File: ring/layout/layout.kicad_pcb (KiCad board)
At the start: 2 copper layers, 31 parts, among them U1 ?, U10 ?, U11 ?, U2 ?, U3 ?, U4 ?, U5 ?, U6 ?, U7 ?, U8 ?, U9 ?, Y1 38.4MHz

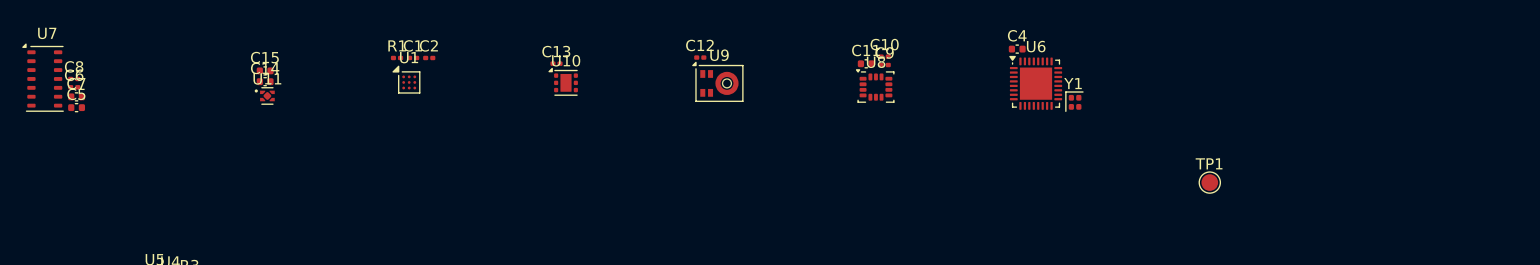
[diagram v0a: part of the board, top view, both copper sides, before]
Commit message: added in rf power
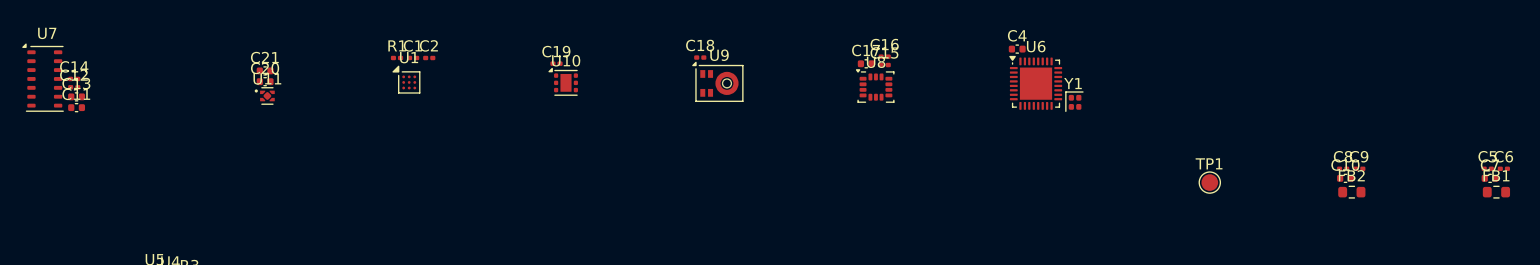
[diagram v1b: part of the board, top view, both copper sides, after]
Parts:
- added C10: 1uF, C_0402_1005Metric:C_0402_1005Metric, F.Cu at (292.2, 114.5)
- added C5: 120pF, C_0201_0603Metric:C_0201_0603Metric, F.Cu at (305.0, 113.6)
- added C6: 100nF, C_0201_0603Metric:C_0201_0603Metric, F.Cu at (306.5, 113.6)
- added C7: 1uF, C_0402_1005Metric:C_0402_1005Metric, F.Cu at (305.3, 114.5)
- added C8: 120pF, C_0201_0603Metric:C_0201_0603Metric, F.Cu at (292.0, 113.6)
- added C9: 100nF, C_0201_0603Metric:C_0201_0603Metric, F.Cu at (293.5, 113.6)
- added FB1: 0 0Hz, R_0603_1608Metric:R_0603_1608Metric, F.Cu at (305.8, 115.7)
- added FB2: 0 0Hz, R_0603_1608Metric:R_0603_1608Metric, F.Cu at (292.8, 115.7)
- renumbered C5 to C11, C6 to C12, C7 to C13, C8 to C14, C9 to C15, C10 to C16, C11 to C17, C12 to C18, C13 to C19, C14 to C20, C15 to C21
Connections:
- net cpu.N259 renamed cpu.N337
- net cpu.N260 renamed cpu.N338
- net cpu.N264 renamed cpu.N342
- U6 pad 10: GND -> cpu.N360
- U6 pad 13: GND -> cpu.N361
- U6 pad 25: GND -> cpu.N392

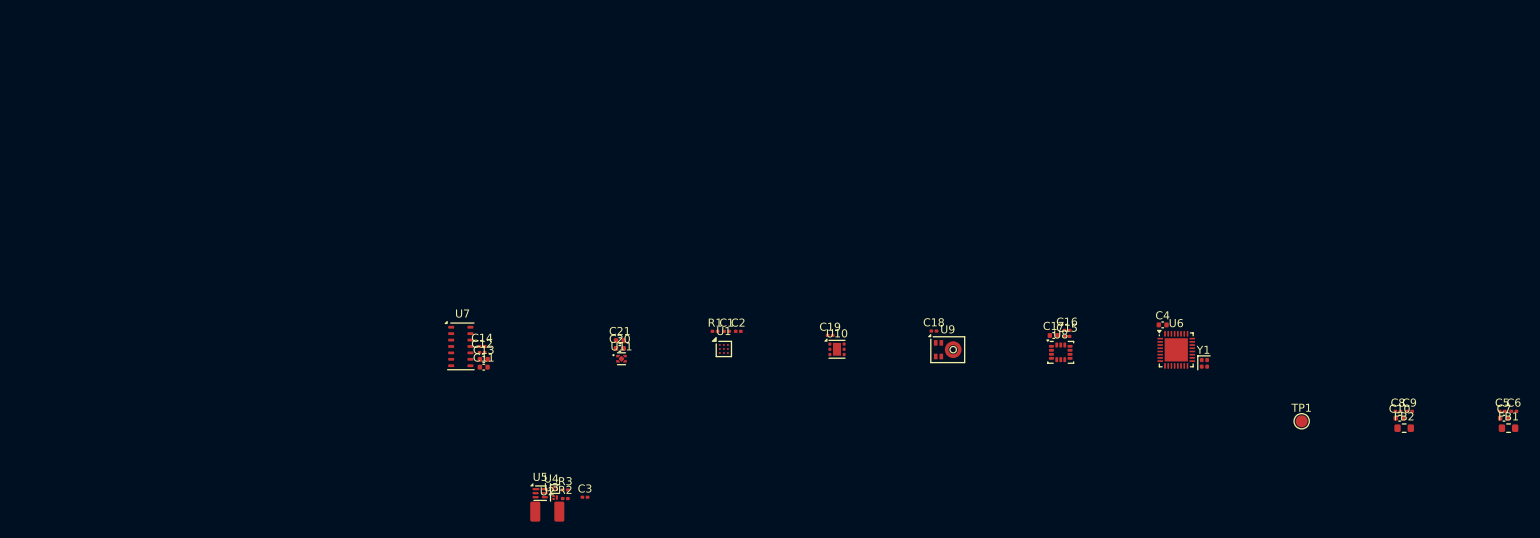
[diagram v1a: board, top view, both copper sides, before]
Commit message: finished port and antenna in zener
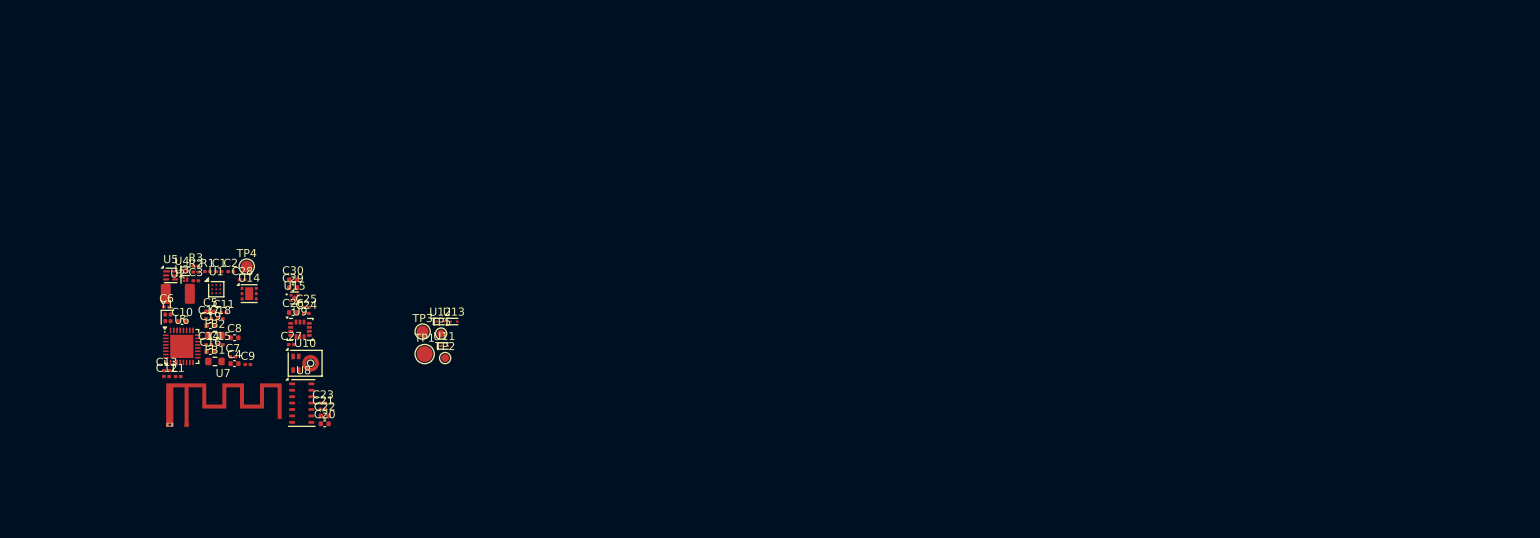
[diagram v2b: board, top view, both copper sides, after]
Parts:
- added C22: 4.7uF, C_0402_1005Metric:C_0402_1005Metric, F.Cu at (158.3, 114.2)
- added C23: 100nF, C_0201_0603Metric:C_0201_0603Metric, F.Cu at (158.0, 112.6)
- added C24: 100nF, C_0201_0603Metric:C_0201_0603Metric, F.Cu at (156.0, 101.4)
- added C25: 100nF, C_0201_0603Metric:C_0201_0603Metric, F.Cu at (156.0, 100.7)
- added C26: 1uF, C_0402_1005Metric:C_0402_1005Metric, F.Cu at (154.3, 101.3)
- added C27: 100nF, C_0201_0603Metric:C_0201_0603Metric, F.Cu at (154.1, 105.3)
- added C28: 100nF, C_0201_0603Metric:C_0201_0603Metric, F.Cu at (148.0, 97.2)
- added C29: 1uF, C_0402_1005Metric:C_0402_1005Metric, F.Cu at (154.3, 98.2)
- added C30: 1uF, C_0402_1005Metric:C_0402_1005Metric, F.Cu at (154.3, 97.3)
- added L1: 3.2nH, L_0201_0603Metric:L_0201_0603Metric, F.Cu at (140.0, 109.3)
- added TP2: , TestPoint_Pad_D1.0mm:TestPoint_Pad_D1.0mm, F.Cu at (173.3, 107.0)
- added TP3: , TestPoint_Pad_D1.5mm:TestPoint_Pad_D1.5mm, F.Cu at (170.5, 103.7)
- added TP4: , TestPoint_Pad_D1.0mm:TestPoint_Pad_D1.0mm, F.Cu at (148.5, 95.6)
- added TP5: , TestPoint_Pad_D1.0mm:TestPoint_Pad_D1.0mm, F.Cu at (172.8, 104.0)
- added U12: ?, D_SOD-923:D_SOD-923, F.Cu at (172.7, 102.5)
- added U13: ?, D_SOD-923:D_SOD-923, F.Cu at (174.4, 102.5)
- added U14: ?, WSON-6-1EP_2x2mm_P0.65mm_EP1x1.6mm:WSON-6-1EP_2x2mm_P0.65mm_EP1x1.6mm, F.Cu at (148.8, 99.0)
- added U15: ?, Texas_X2SON-4_1x1mm_P0.65mm:Texas_X2SON-4_1x1mm_P0.65mm, F.Cu at (154.5, 99.5)
- C11: value 10uF -> 100nF; footprint C_0402_1005Metric:C_0402_1005Metric -> C_0201_0603Metric:C_0201_0603Metric
- C12: value 100nF -> 1.6pF
- C13: value 4.7uF -> 18pF; footprint C_0402_1005Metric:C_0402_1005Metric -> C_0201_0603Metric:C_0201_0603Metric
- C14: value 100nF -> 120pF
- C16, C19: value 100nF -> 1uF; footprint C_0201_0603Metric:C_0201_0603Metric -> C_0402_1005Metric:C_0402_1005Metric
- C17: value 1uF -> 120pF; footprint C_0402_1005Metric:C_0402_1005Metric -> C_0201_0603Metric:C_0201_0603Metric
- C20: value 1uF -> 10uF
- C21, C7: value 1uF -> 100nF; footprint C_0402_1005Metric:C_0402_1005Metric -> C_0201_0603Metric:C_0201_0603Metric
- C5: value 120pF -> 10uF; footprint C_0201_0603Metric:C_0201_0603Metric -> C_0402_1005Metric:C_0402_1005Metric
- C8: value 120pF -> 1uF; footprint C_0201_0603Metric:C_0201_0603Metric -> C_0402_1005Metric:C_0402_1005Metric
- C9: value 100nF -> 10nF
- TP1: footprint TestPoint_Pad_D1.5mm:TestPoint_Pad_D1.5mm -> TestPoint_Pad_D2.0mm:TestPoint_Pad_D2.0mm
- U10: footprint WSON-6-1EP_2x2mm_P0.65mm_EP1x1.6mm:WSON-6-1EP_2x2mm_P0.65mm_EP1x1.6mm -> Infineon_PG-LLGA-5-1:Infineon_PG-LLGA-5-1
- U11: footprint Texas_X2SON-4_1x1mm_P0.65mm:Texas_X2SON-4_1x1mm_P0.65mm -> D_SOD-923:D_SOD-923
- U7: footprint Maxim_OLGA-14_3.3x5.6mm_P0.8mm:Maxim_OLGA-14_3.3x5.6mm_P0.8mm -> Texas_SWRA117D_2.4GHz_Right:Texas_SWRA117D_2.4GHz_Right
- U8: footprint LGA-14_3x2.5mm_P0.5mm_LayoutBorder3x4y:LGA-14_3x2.5mm_P0.5mm_LayoutBorder3x4y -> Maxim_OLGA-14_3.3x5.6mm_P0.8mm:Maxim_OLGA-14_3.3x5.6mm_P0.8mm
- U9: footprint Infineon_PG-LLGA-5-1:Infineon_PG-LLGA-5-1 -> LGA-14_3x2.5mm_P0.5mm_LayoutBorder3x4y:LGA-14_3x2.5mm_P0.5mm_LayoutBorder3x4y
- moved C6 168.5 mm to (138.5, 100.6)
- moved C5 161.5 mm to (144.0, 101.2)
- moved FB1 161.5 mm to (144.6, 107.4)
- moved C7 158.6 mm to (146.8, 106.8)
- moved C10 152.2 mm to (140.5, 102.4)
- moved FB2 148.7 mm to (144.6, 104.2)
- moved C8 145.3 mm to (147.0, 104.5)
- moved C9 144.9 mm to (148.7, 107.8)
- moved Y1 129.3 mm to (138.7, 102.0)
- moved U6 124.0 mm to (140.4, 105.6)
- moved C4 115.8 mm to (147.0, 107.7)
- moved TP1 109.6 mm to (170.7, 106.5)
- moved C16 106.8 mm to (144.0, 106.2)
- moved C15 105.6 mm to (145.2, 105.3)
- moved C17 105.4 mm to (143.8, 102.1)
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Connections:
- net N56 renamed N64
- net batman.N85 renamed batman.N93
- net batman.N86 renamed batman.N94
- net battery.N43 renamed battery.N51
- net battery.N44 renamed battery.N52
- net battery.N45 renamed battery.N53
- net battery.N46 renamed battery.N54
- net battery.N47 renamed battery.N55
- net battery.N48 renamed battery.N56
- net battery.N49 renamed battery.N57
- net cpu.N337 renamed cpu.N394
- net cpu.N338 renamed cpu.N395
- net cpu.N342 renamed cpu.N399
- net cpu.N392 renamed cpu.N498
- C10 pad 1: cpu.N360 -> VDD
- C11 pad 1: VBATT -> VDD
- C12 pad 1: VBATT -> cpu.ant.N487
- C13 pad 1: VDD -> cpu.ant.N488
- C13 pad 2: GND -> cpu.ant.N489
- C14 pad 1: VDD -> cpu.N418
- C15 pad 1: VDD -> cpu.N418
- C16 pad 1: VDD -> cpu.N418
- C17 pad 1: VDD -> cpu.N417
- C18 pad 1: VDD -> cpu.N417
- C19 pad 1: VDD -> cpu.N417
- C21 pad 1: VDD -> VBATT
- C5 pad 1: cpu.N361 -> VDD
- C6 pad 1: cpu.N361 -> VDD
- C7 pad 1: cpu.N361 -> VDD
- C8 pad 1: cpu.N360 -> VDD
- C9 pad 1: cpu.N360 -> VDD
- FB1 pad 2: cpu.N361 -> cpu.N418
- FB2 pad 2: cpu.N360 -> cpu.N417
- U10 pad 1: SCL -> N174
- U10 pad 2: GND -> VDD
- U10 pad 3: N111 -> N173
- U10 pad 5: VDD -> GND
- U11 pad 1: VDD -> VBATT
- U6 pad 10: cpu.N360 -> cpu.N417
- U6 pad 12: GND -> cpu.N463
- U6 pad 13: cpu.N361 -> cpu.N418
- U6 pad 31: N165 -> N173
- U6 pad 32: N166 -> N174
- U7 pad 1: hbt.N137 -> cpu.ant.N489
- U7 pad 2: SCL -> GND
- U8 pad 1: GND -> hbt.N145
- U8 pad 10: imu.N217 -> VBATT
- U8 pad 11: imu.N218 -> VDD
- U8 pad 12: VDD -> GND
- U8 pad 13: SCL -> N119
- U8 pad 14: SDA -> hbt.N145
- U8 pad 2: GND -> SCL
- U8 pad 3: GND -> SDA
- U8 pad 4: N187 -> GND
- U8 pad 5: VDD -> hbt.N145
- U8 pad 6: GND -> hbt.N145
- U8 pad 7: GND -> hbt.N145
- U8 pad 8: VDD -> hbt.N145
- U8 pad 9: N188 -> VBATT
- U9 pad 1: N166 -> GND
- U9 pad 2: VDD -> GND
- U9 pad 3: N165 -> GND
- U9 pad 4: GND -> N195
- U9 pad 5: GND -> VDD

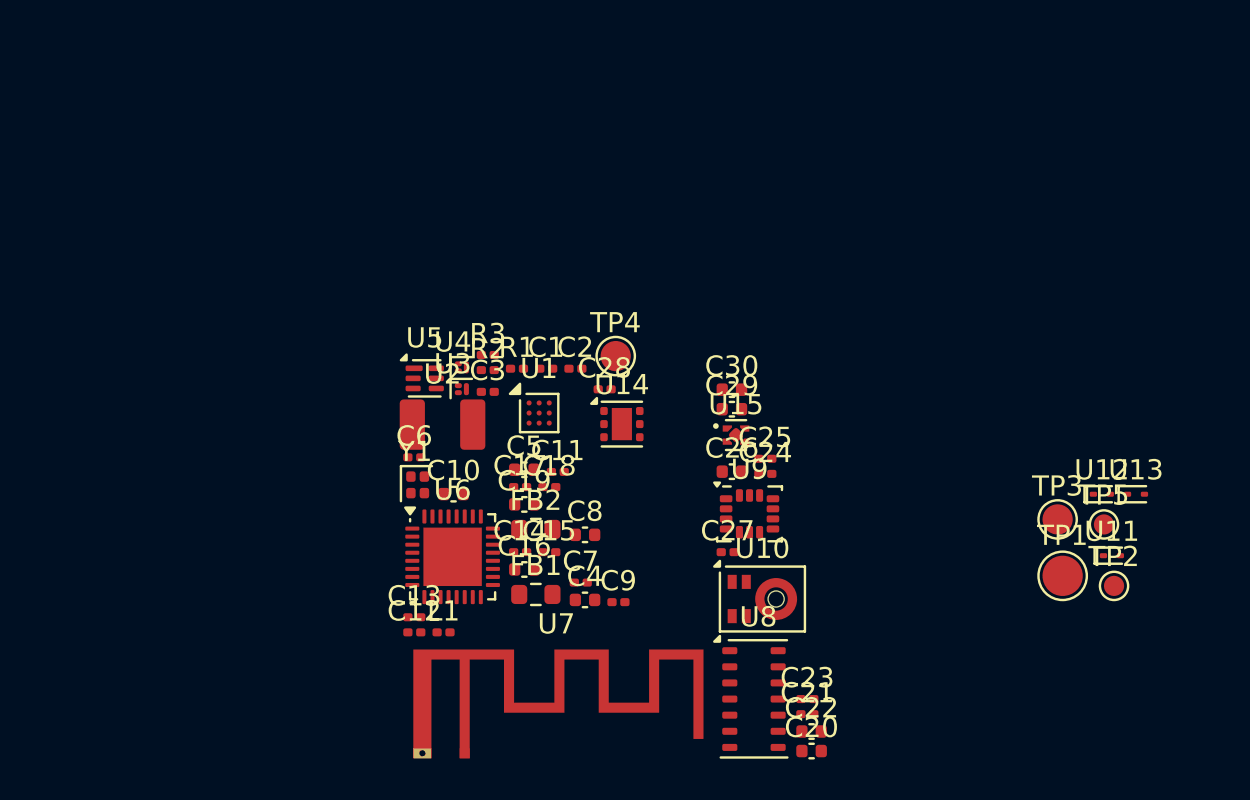
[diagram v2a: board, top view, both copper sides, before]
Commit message: laid out pcb and began routing (6.2mm tall!)
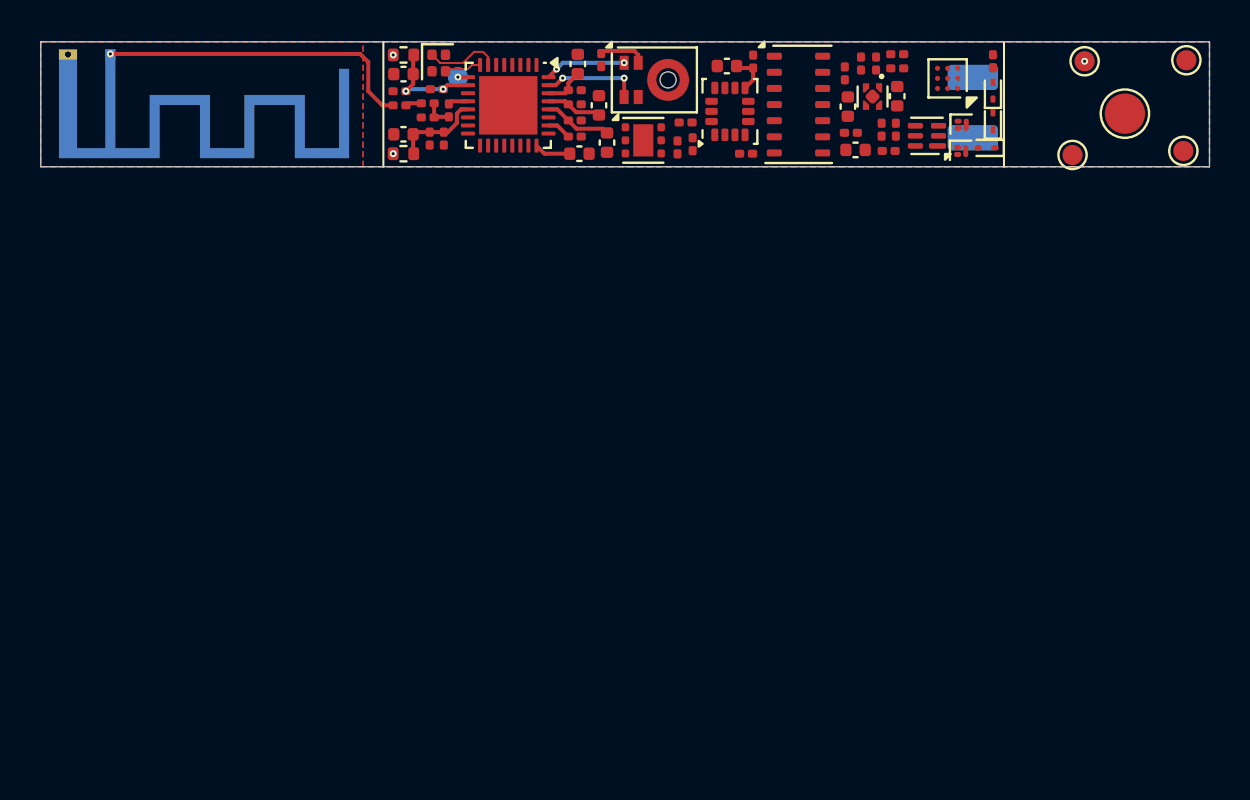
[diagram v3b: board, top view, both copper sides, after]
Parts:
- added C31: 1uF, C_0201_0603Metric:C_0201_0603Metric, F.Cu at (160.7, 81.1)
- added L2: 3.2nH, L_0201_0603Metric:L_0201_0603Metric, F.Cu at (139.2, 83.0)
- added R4: 2.2k, R_0201_0603Metric:R_0201_0603Metric, F.Cu at (162.1, 85.4)
- added R5: 330, R_0201_0603Metric:R_0201_0603Metric, F.Cu at (161.7, 84.4)
- added TP6: , TestPoint_Pad_D1.0mm:TestPoint_Pad_D1.0mm, F.Cu at (171.8, 81.0)
- C30: footprint C_0402_1005Metric:C_0402_1005Metric -> C_0201_0603Metric:C_0201_0603Metric
- FB1, FB2: footprint R_0603_1608Metric:R_0603_1608Metric -> R_0402_1005Metric:R_0402_1005Metric
- L1: value 3.2nH -> 2nH
- R1: value 10k -> 4.7k
- R2: value 2.2k -> 4.7k
- R3: value 330 -> 10k
- TP1: footprint TestPoint_Pad_D2.0mm:TestPoint_Pad_D2.0mm -> TestPoint_Pad_D1.0mm:TestPoint_Pad_D1.0mm; moved to B.Cu
- TP2: footprint TestPoint_Pad_D1.0mm:TestPoint_Pad_D1.0mm -> TestPoint_Pad_D2.0mm:TestPoint_Pad_D2.0mm
- TP3: footprint TestPoint_Pad_D1.5mm:TestPoint_Pad_D1.5mm -> TestPoint_Pad_D1.0mm:TestPoint_Pad_D1.0mm
- U2, U7: moved to B.Cu
- moved TP1 38.9 mm to (140.7, 81.8)
- moved U7 38.9 mm to (123.5, 80.6)
- moved TP4 31.9 mm to (176.9, 80.9)
- moved C23 31.1 mm to (159.9, 81.6), turned to 90 degrees
- moved C22 31.1 mm to (160.1, 83.2), turned to -90 degrees
- moved U2 30.7 mm to (166.3, 83.3), turned to 90 degrees
- moved C20 29.9 mm to (160.4, 85.4)
- moved U8 29.6 mm to (157.6, 83.1)
- moved R3 29.0 mm to (167.3, 81.0), turned to 90 degrees
- moved C21 28.9 mm to (160.2, 84.5)
- moved U3 28.1 mm to (165.7, 84.1)
- moved U5 27.7 mm to (164.0, 84.7), turned to 180 degrees
- moved U4 27.0 mm to (165.7, 85.4)
- moved U10 26.3 mm to (150.4, 81.9)
- moved U1 26.2 mm to (165.0, 81.8), turned to 180 degrees
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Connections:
- net N173 renamed mic_clk
- net N174 renamed mic_data
- net batman.N93 renamed batman.batman_vdd_out
- net battery.N51 renamed battery.bat_cout
- net battery.N52 renamed battery.bat_dout
- net battery.N55 renamed battery.bat_vss
- net battery.N56 renamed battery.N59
- net battery.N57 renamed battery.bat_qm
- net cpu.N394 renamed cpu.xin
- net cpu.N395 renamed cpu.xout
- net cpu.N399 renamed cpu.decouple
- net cpu.N417 renamed cpu.rfvdd
- net cpu.N418 renamed cpu.pavdd
- net cpu.N463 renamed cpu.ant
- net cpu.N498 renamed cpu.N520
- net cpu.ant.N489 renamed cpu.ant.out3
- net hbt.N145 renamed hbt.N152
- net imu.N225 renamed imu.N232
- net imu.N226 renamed imu.N233
- C12 pad 1: cpu.ant.N487 -> cpu.ant.out1
- C13 pad 1: cpu.ant.N488 -> cpu.ant.out2
- C3 pad 1: battery.N54 -> battery.bat2
- L1 pad 2: cpu.ant.N488 -> cpu.ant.out1
- R1 pad 1: batman.N94 -> VDD
- R1 pad 2: GND -> sda
- R2 pad 1: battery.N53 -> VDD
- R2 pad 2: GND -> scl
- R3 pad 1: VBATT -> batman.bin
- R3 pad 2: battery.N54 -> GND
- TP1 pad 1: VBATT -> rst
- TP2 pad 1: SDA -> VBATT
- TP3 pad 1: SCL -> sda
- TP4 pad 1: GND -> scl
- U1 pad A1: N64 -> bat_low
- U1 pad A2: SDA -> sda
- U1 pad A3: SCL -> scl
- U1 pad B1: batman.N94 -> batman.bin
- U12 pad 1: SDA -> sda
- U13 pad 1: SCL -> scl
- U14 pad 1: SCL -> scl
- U14 pad 3: N119 -> tmp_int
- U14 pad 6: SDA -> sda
- U5 pad 5: battery.N54 -> battery.bat2
- U5 pad 6: battery.N53 -> battery.bat_vm
- U6 pad 1: GND -> bat_low
- U6 pad 14: GND -> N381
- U6 pad 15: GND -> N380
- U6 pad 16: GND -> imu_int1
- U6 pad 17: GND -> tmp_int
- U6 pad 18: GND -> N382
- U6 pad 19: GND -> N383
- U6 pad 2: GND -> hbt_int
- U6 pad 20: GND -> N384
- U6 pad 21: GND -> N385
- U6 pad 22: GND -> N386
- U6 pad 23: GND -> N387
- U6 pad 3: GND -> imu_int2
- U6 pad 4: GND -> sda
- U6 pad 5: GND -> scl
- U6 pad 6: GND -> N379
- U6 pad 9: GND -> rst
- U8 pad 13: N119 -> hbt_int
- U8 pad 2: SCL -> scl
- U8 pad 3: SDA -> sda
- U9 pad 13: SCL -> scl
- U9 pad 14: SDA -> sda
- U9 pad 4: N195 -> imu_int1
- U9 pad 9: N196 -> imu_int2
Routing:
- net cpu.ant.out3: track 0.00 -> 15.9 mm, vias 0 -> 1
- net VDD: track 0.00 -> 13.8 mm, vias 0 -> 2
- net cpu.rfvdd: track 0.00 -> 5.17 mm, vias 0 -> 2
- net mic_clk: track 0.00 -> 4.83 mm, vias 0 -> 2
- net cpu.pavdd: track 0.00 -> 4.49 mm
- net mic_data: track 0.00 -> 4.05 mm, vias 0 -> 2
- net cpu.xin: track 0.00 -> 3.69 mm
- net cpu.xout: track 0.00 -> 1.84 mm
- net cpu.decouple: track 0.00 -> 1.82 mm
- net cpu.ant.out1: track 0.00 -> 1.44 mm
- net cpu.ant: track 0.00 -> 1.00 mm
- net cpu.ant.out2: track 0.00 -> 0.80 mm
- net rst: track 0.00 -> 0.50 mm, vias 0 -> 1
- net GND: vias 0 -> 1
- added copper zone on B.Cu, net GND
- added copper zone on F.Cu, net GND
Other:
- board outline added: 58 x 6.2 mm
- rule pad_to_mask_clearance: 0 -> 0.1
- board text added: "we get 6.28 * (dist off finger) extra length!"
